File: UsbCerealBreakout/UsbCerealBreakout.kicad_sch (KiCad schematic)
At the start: 3 parts, among them J1 Serial Connector, J2 USB_C_Data_Output, P1 USB_C_Plug

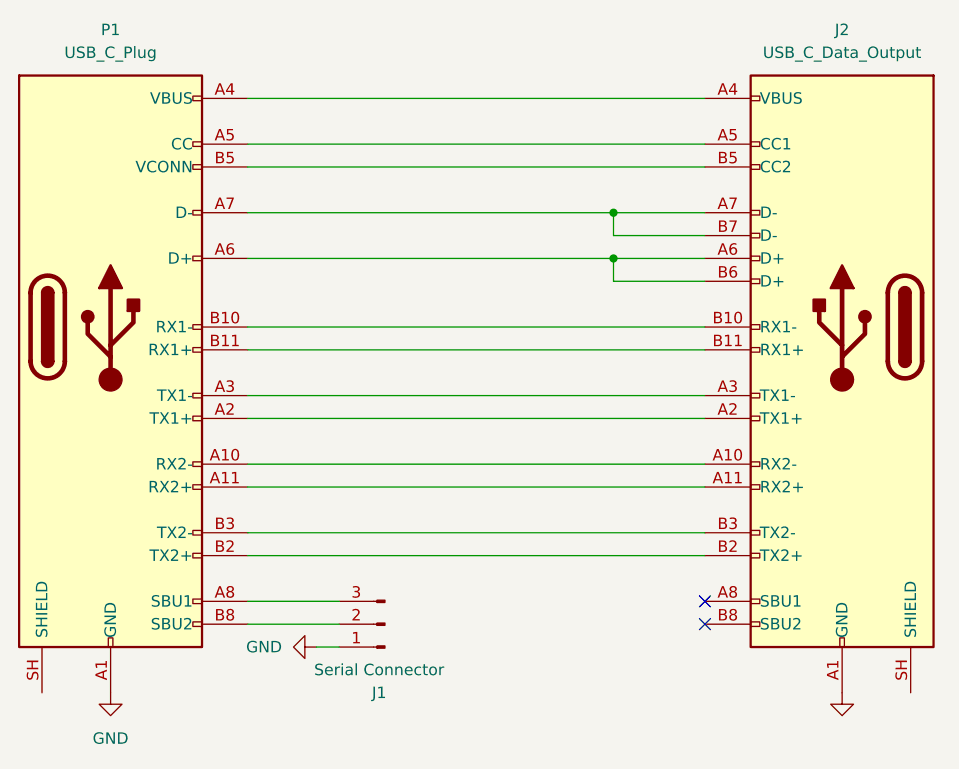
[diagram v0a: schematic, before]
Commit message: Route the PCB, it may have some DRC issues and incorrect thickness for the USB-C plug connector
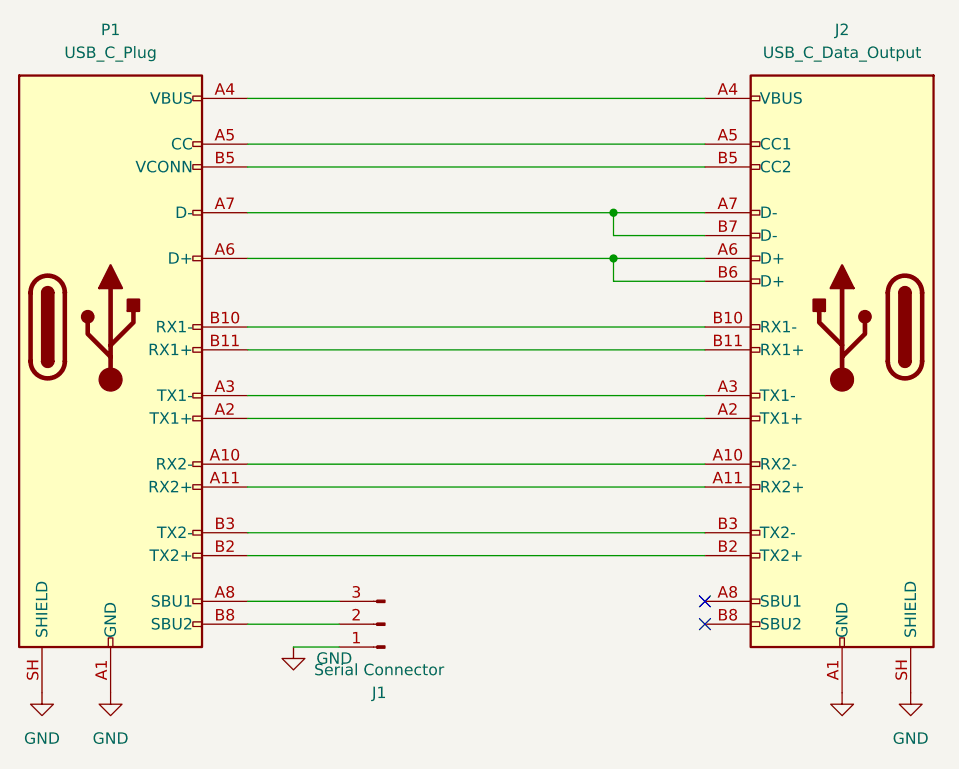
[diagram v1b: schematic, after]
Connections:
- net GND: now also J2.SH (SHIELD), P1.SH (SHIELD)
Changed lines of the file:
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@@
 	(wire
 		(pts
-			(xy 91.44 83.82) (xy 93.98 83.82)
+			(xy 88.9 83.82) (xy 93.98 83.82)
 		)
 		(stroke
@@
 			(width 0)
 			(type default)
+		)
+	)
+	(symbol
+		(lib_id "power:GND")
+		(at 60.96 88.9 0)
+		(unit 1)
+		(body_style 1)
+		(exclude_from_sim no)
+		(in_bom yes)
+		(on_board yes)
+		(in_pos_files yes)
+		(dnp no)
+		(fields_autoplaced yes)
+		(property "Reference" "#PWR04"
+			(at 60.96 95.25 0)
+			(hide yes)
+			(show_name no)
+			(do_not_autoplace no)
+			(effects
+				(font
+					(size 1.27 1.27)
+				)
+			)
+		)
+		(property "Value" "GND"
+			(at 60.96 93.98 0)
+			(show_name no)
+			(do_not_autoplace no)
+			(effects
+				(font
+					(size 1.27 1.27)
+				)
+			)
+		)
+		(property "Footprint" ""
+			(at 60.96 88.9 0)
+			(hide yes)
+			(show_name no)
+			(do_not_autoplace no)
+			(effects
+				(font
+					(size 1.27 1.27)
+				)
+			)
+		)
+		(property "Datasheet" ""
+			(at 60.96 88.9 0)
+			(hide yes)
+			(show_name no)
+			(do_not_autoplace no)
+			(effects
+				(font
+					(size 1.27 1.27)
+				)
+			)
+		)
+		(property "Description" "Power symbol creates a global label with name \"GND\" , ground"
+			(at 60.96 88.9 0)
+			(hide yes)
+			(show_name no)
+			(do_not_autoplace no)
+			(effects
+				(font
+					(size 1.27 1.27)
+				)
+			)
+		)
+		(pin "1"
+		)
+		(instances
+			(project "UsbCerealBreakout"
+				(path "/4f3cc564-d206-4b89-a7c8-27fc89fac8d6"
+					(reference "#PWR04")
+					(unit 1)
+				)
+			)
 		)
 	)
@@
 	)
 	(symbol
+		(lib_id "power:GND")
+		(at 157.48 88.9 0)
+		(unit 1)
+		(body_style 1)
+		(exclude_from_sim no)
+		(in_bom yes)
+		(on_board yes)
+		(in_pos_files yes)
+		(dnp no)
+		(fields_autoplaced yes)
+		(property "Reference" "#PWR05"
+			(at 157.48 95.25 0)
+			(hide yes)
+			(show_name no)
+			(do_not_autoplace no)
+			(effects
+				(font
+					(size 1.27 1.27)
+				)
+			)
+		)
+		(property "Value" "GND"
+			(at 157.48 93.98 0)
+			(show_name no)
+			(do_not_autoplace no)
+			(effects
+				(font
+					(size 1.27 1.27)
+				)
+			)
+		)
+		(property "Footprint" ""
+			(at 157.48 88.9 0)
+			(hide yes)
+			(show_name no)
+			(do_not_autoplace no)
+			(effects
+				(font
+					(size 1.27 1.27)
+				)
+			)
+		)
+		(property "Datasheet" ""
+			(at 157.48 88.9 0)
+			(hide yes)
+			(show_name no)
+			(do_not_autoplace no)
+			(effects
+				(font
+					(size 1.27 1.27)
+				)
+			)
+		)
+		(property "Description" "Power symbol creates a global label with name \"GND\" , ground"
+			(at 157.48 88.9 0)
+			(hide yes)
+			(show_name no)
+			(do_not_autoplace no)
+			(effects
+				(font
+					(size 1.27 1.27)
+				)
+			)
+		)
+		(pin "1"
+		)
+		(instances
+			(project "UsbCerealBreakout"
+				(path "/4f3cc564-d206-4b89-a7c8-27fc89fac8d6"
+					(reference "#PWR05")
+					(unit 1)
+				)
+			)
+		)
+	)
+	(symbol
 		(lib_id "Connector:USB_C_Receptacle")
 		(at 149.86 48.26 0)
@@
 	(symbol
 		(lib_id "power:GND")
-		(at 91.44 83.82 270)
+		(at 88.9 83.82 0)
 		(unit 1)
 		(body_style 1)
@@
 		(fields_autoplaced yes)
 		(property "Reference" "#PWR03"
-			(at 85.09 83.82 0)
+			(at 88.9 90.17 0)
 			(hide yes)
 			(show_name no)
@@
 		)
 		(property "Value" "GND"
-			(at 87.63 83.8199 90)
-			(show_name no)
-			(do_not_autoplace no)
-			(effects
-				(font
-					(size 1.27 1.27)
-				)
-				(justify right)
+			(at 91.44 85.0899 0)
+			(show_name no)
+			(do_not_autoplace no)
+			(effects
+				(font
+					(size 1.27 1.27)
+				)
+				(justify left)
 			)
 		)
 		(property "Footprint" ""
-			(at 91.44 83.82 0)
+			(at 88.9 83.82 0)
 			(hide yes)
 			(show_name no)
@@
 		)
 		(property "Datasheet" ""
-			(at 91.44 83.82 0)
+			(at 88.9 83.82 0)
 			(hide yes)
 			(show_name no)
@@
 		)
 		(property "Description" "Power symbol creates a global label with name \"GND\" , ground"
-			(at 91.44 83.82 0)
-			(hide yes)
-			(show_name no)
+			(at 88.9 83.82 0)
+			(hide yes)
+			(show_name no)

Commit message: Switch to Molex USB-C plug that is actually in stock
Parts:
- P1: footprint Connector_USB:USB_C_Plug_JAE_DX07P024AJ1 -> Connector_USB:USB_C_Plug_Molex_105444
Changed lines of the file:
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@@
 			)
 		)
-		(property "Footprint" "Connector_USB:USB_C_Plug_JAE_DX07P024AJ1"
+		(property "Footprint" "Connector_USB:USB_C_Plug_Molex_105444"
 			(at 72.39 48.26 0)
 			(hide yes)

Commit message: Slight updates to fix branch problems, added VBUS via at USB connector
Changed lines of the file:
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@@
 		(in_pos_files yes)
 		(dnp no)
-		(fields_autoplaced yes)
 		(property "Reference" "#PWR03"
 			(at 88.9 90.17 0)
@@
 		)
 		(property "Value" "GND"
-			(at 91.44 85.0899 0)
+			(at 83.058 84.8359 0)
 			(show_name no)
 			(do_not_autoplace no)
